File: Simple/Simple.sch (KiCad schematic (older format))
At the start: 33 parts, among them J1 IR1, J10 Conn_01x02_Female, J11 Motor1, J12 Motor2, J13 Conn_01x03_Male, J14 Conn_01x04_Male, J2 IR2, J3 IR3, J4 IR4, J5 Conn_01x03_Male, J6 Conn_01x02_Female, J7 Ultra1, J8 Ultra2, J9 Conn_01x03_Male, Q1 BSS138, Q2 BSS138, SW1 SW_Push, U1 AP7366, U2 SP485CN-L_TR, U3 ATtiny816-SS

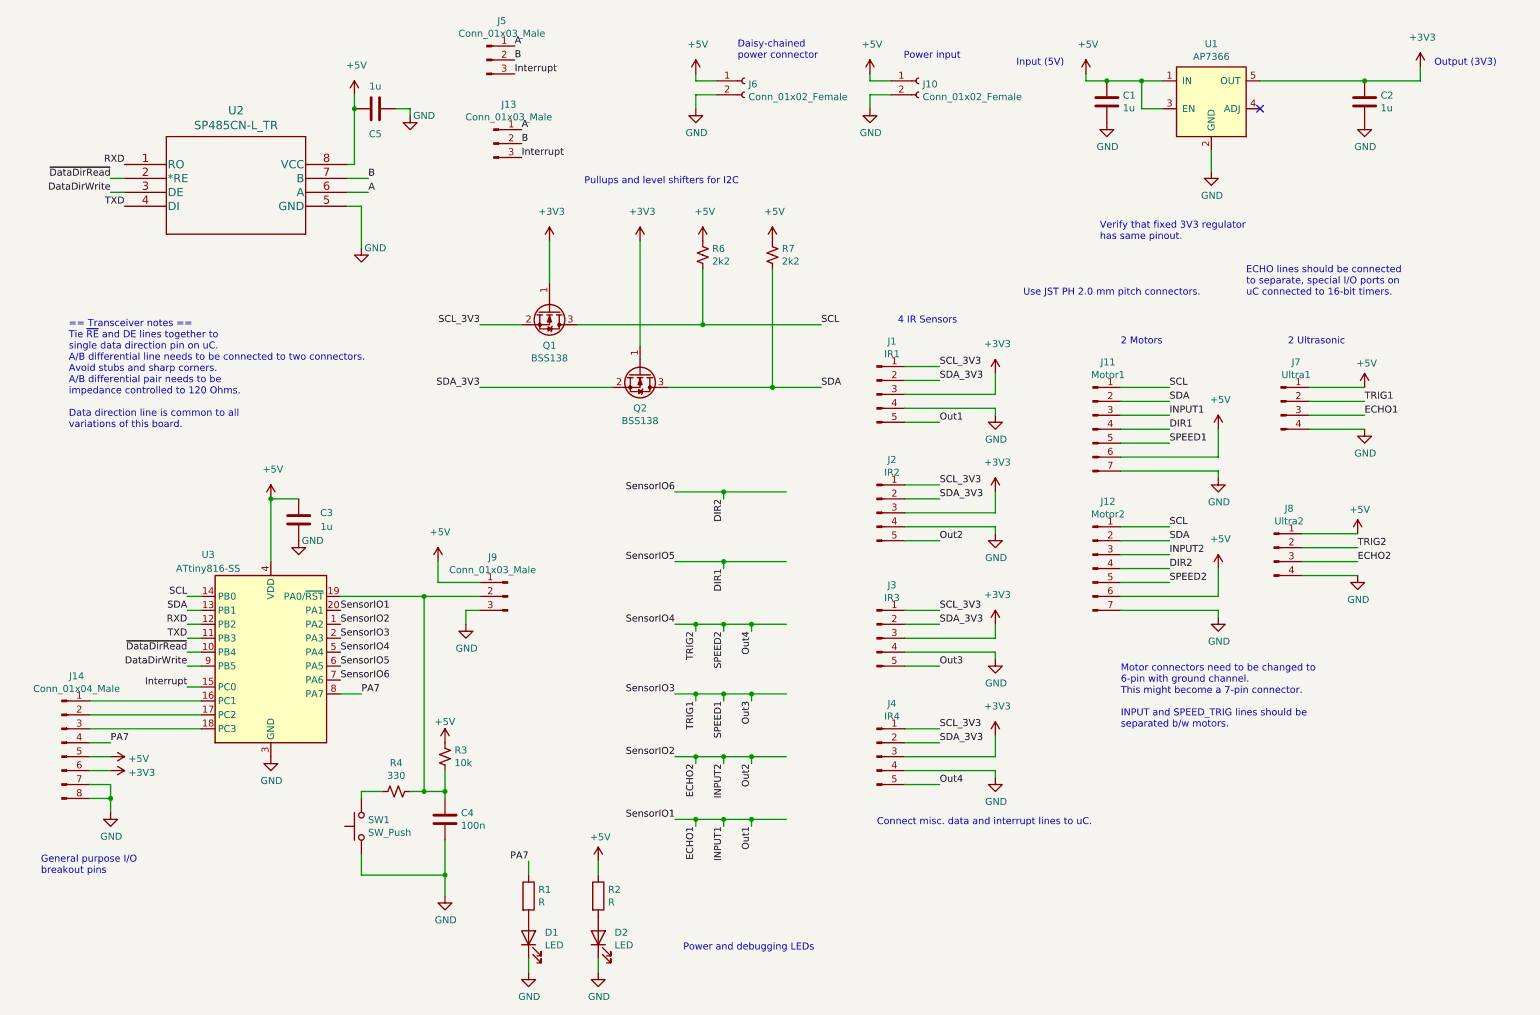
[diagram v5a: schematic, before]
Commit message: Layout started and sensor connectors are connected to eachother but not microcontroller
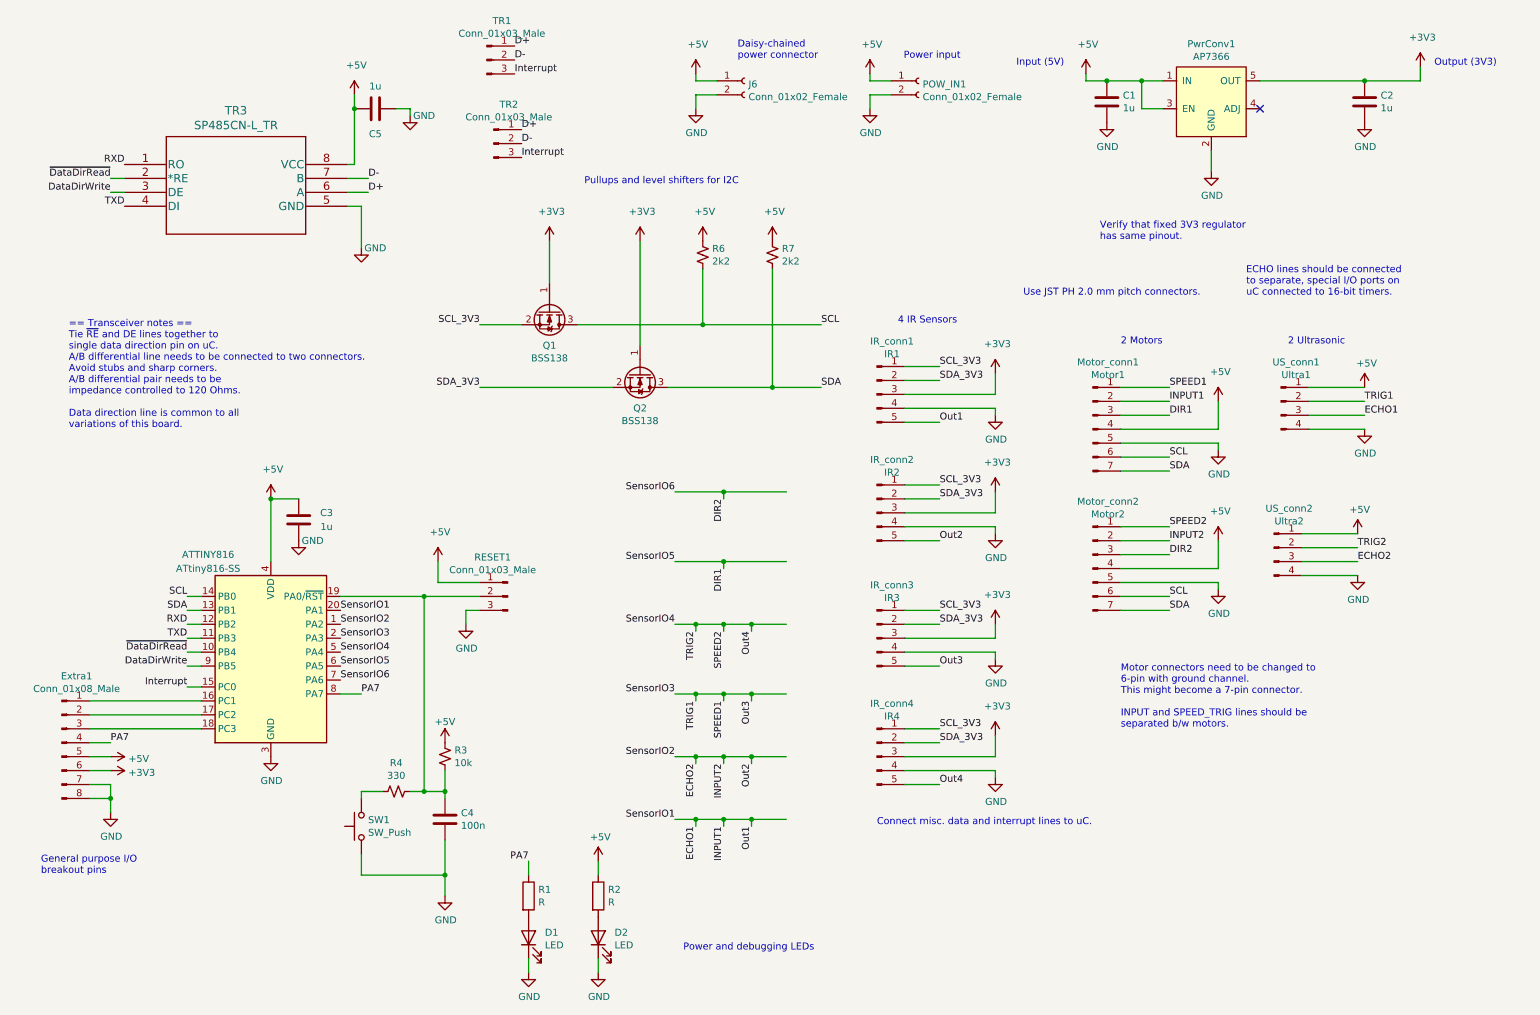
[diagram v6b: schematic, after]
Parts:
- ATTINY816: renamed from U3; footprint Package_SO:SOIC-14_3.9x8.7mm_P1.27mm -> Package_SO:SOIC-20W_7.5x12.8mm_P1.27mm
- Extra1: renamed from J14; value Conn_01x04_Male -> Conn_01x08_Male; footprint Connector_JST:JST_PH_B4B-PH-K_1x04_P2.00mm_Vertical -> Connector_JST:JST_PH_B8B-PH-K_1x08_P2.00mm_Vertical
- SW1: footprint (none) -> SimpleUCLib:SW_SPST_PTS815
- renumbered J1 to IR_conn1, J2 to IR_conn2, J3 to IR_conn3, J4 to IR_conn4, J11 to Motor_conn1, J12 to Motor_conn2, J10 to POW_IN1, U1 to PwrConv1, J9 to RESET1, J5 to TR1, J13 to TR2, U2 to TR3, J7 to US_conn1, J8 to US_conn2
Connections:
- net labels added: D+, D-
- net labels removed: A, B

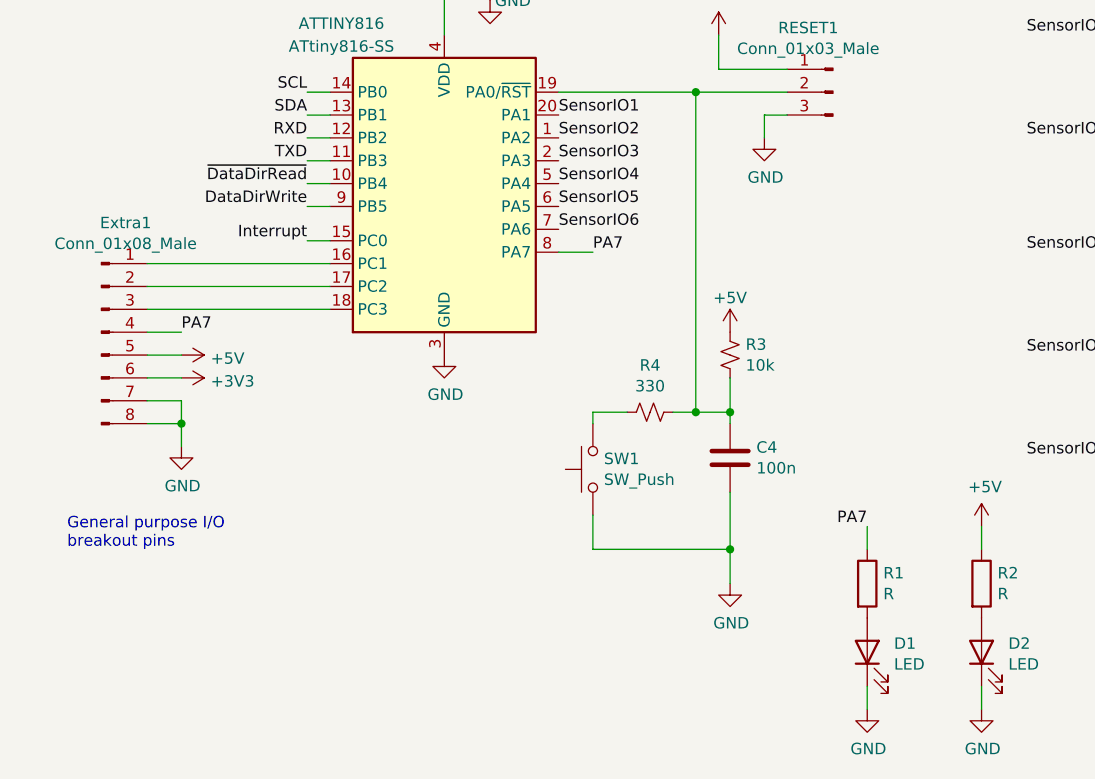
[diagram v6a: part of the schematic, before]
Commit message: rotated motor/ultrasonic connectors and added traces for all but pwr, gnd, d+/-
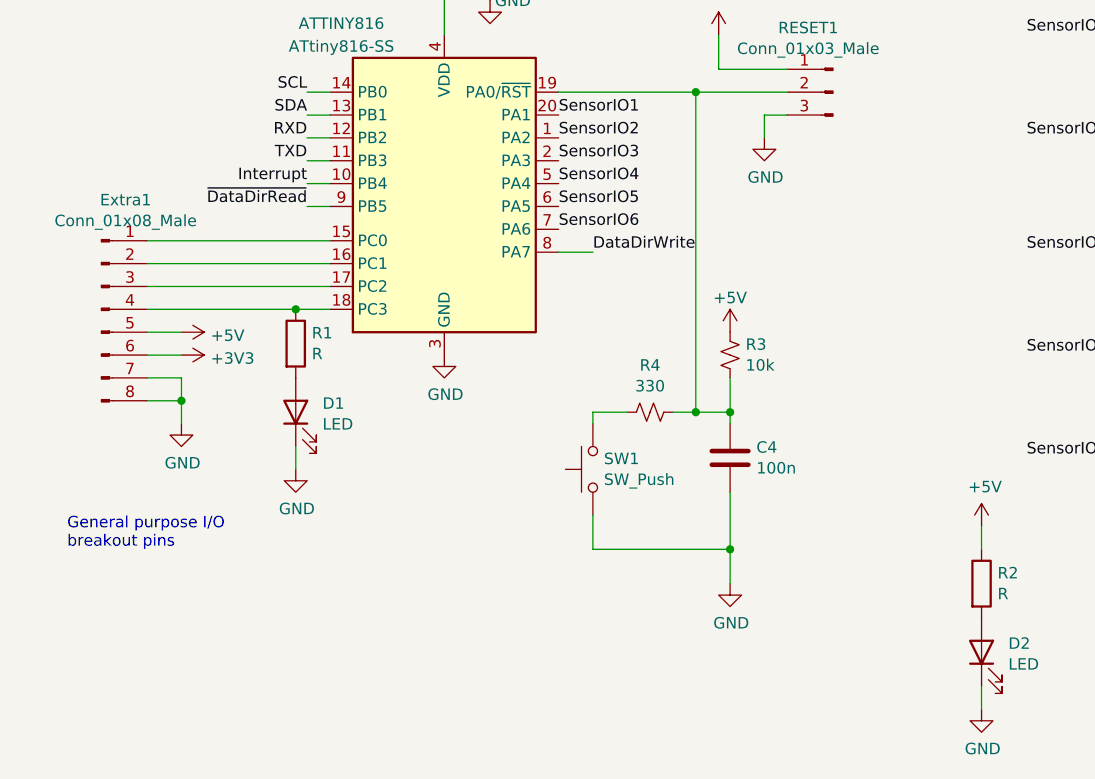
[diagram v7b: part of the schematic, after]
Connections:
- net labels removed: PA7
- wire segments 168 -> 167
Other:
- moved on the sheet: D1, Extra1, R1
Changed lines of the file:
@@
 Text Label 5200 4500 2    50   ~ 0
 SensorIO5
-Text Label 1700 5150 2    50   ~ 0
+Text Label 1700 5250 2    50   ~ 0
 ~DataDirRead
 Text Label 5200 4950 2    50   ~ 0
@@
 Text Label 4100 1600 0    50   ~ 0
 Interrupt
-Text Label 1700 5400 2    50   ~ 0
-Interrupt
 Text Label 1150 1850 2    50   ~ 0
 DataDirWrite
@@
 	1    0    0    -1
 $EndComp
-Text Label 1700 5250 2    50   ~ 0
+Text Label 2950 5450 0    50   ~ 0
 DataDirWrite
 Wire Wire Line
@@
 Wire Wire Line
 	1800 5150 1700 5150
-Wire Wire Line
-	1700 5400 1800 5400
 $Comp
 L Connector:Conn_01x08_Male Extra1
 U 1 1 6057FB03
-P 800 5800
-F 0 "Extra1" H 906 6278 50  0000 C CNN
-F 1 "Conn_01x08_Male" H 906 6187 50  0000 C CNN
-F 2 "Connector_JST:JST_PH_B8B-PH-K_1x08_P2.00mm_Vertical" H 800 5800 50  0001 C CNN
-F 3 "~" H 800 5800 50  0001 C CNN
-	1    800  5800
+P 800 5700
+F 0 "Extra1" H 906 6178 50  0000 C CNN
+F 1 "Conn_01x08_Male" H 906 6087 50  0000 C CNN
+F 2 "Connector_JST:JST_PH_B8B-PH-K_1x08_P2.00mm_Vertical" H 800 5700 50  0001 C CNN
+F 3 "~" H 800 5700 50  0001 C CNN
+	1    800  5700
 	1    0    0    -1
 $EndComp
@@
 	1800 5600 1000 5600
 Wire Wire Line
-	1000 5700 1800 5700
-Wire Wire Line
-	1000 5800 1150 5800
-Text Label 1150 5800 0    50   ~ 0
-PA7
+	1000 5700 1650 5700
 Wire Wire Line
 	2800 5450 2950 5450
-Text Label 2950 5450 0    50   ~ 0
-PA7
+Text Label 1700 5150 2    50   ~ 0
+Interrupt
 Text Notes 650  6750 0    50   ~ 0
 General purpose I/O \nbreakout pins
@@
 Daisy-chained \npower connector
 Wire Wire Line
-	1000 5900 1150 5900
-Wire Wire Line
-	1150 6000 1000 6000
-Wire Wire Line
-	1000 6100 1150 6100
+	1000 5800 1150 5800
+Wire Wire Line
+	1150 5900 1000 5900
+Wire Wire Line
+	1000 6000 1150 6000
+Wire Wire Line
+	1150 6000 1150 6100
+Wire Wire Line
+	1150 6100 1000 6100
+Connection ~ 1150 6100
 Wire Wire Line
 	1150 6100 1150 6200
-Wire Wire Line
-	1150 6200 1000 6200
-Connection ~ 1150 6200
-Wire Wire Line
-	1150 6200 1150 6300
 $Comp
 L power:GND #PWR05
 U 1 1 605D578E
-P 1150 6300
-F 0 "#PWR05" H 1150 6050 50  0001 C CNN
-F 1 "GND" H 1155 6127 50  0000 C CNN
-F 2 "" H 1150 6300 50  0001 C CNN
-F 3 "" H 1150 6300 50  0001 C CNN
-	1    1150 6300
+P 1150 6200
+F 0 "#PWR05" H 1150 5950 50  0001 C CNN
+F 1 "GND" H 1155 6027 50  0000 C CNN
+F 2 "" H 1150 6200 50  0001 C CNN
+F 3 "" H 1150 6200 50  0001 C CNN
+	1    1150 6200
 	1    0    0    -1
 $EndComp
@@
 L power:+5V #PWR03
 U 1 1 605D5831
+P 1150 5800
+F 0 "#PWR03" H 1150 5650 50  0001 C CNN
+F 1 "+5V" V 1165 5928 50  0000 L CNN
+F 2 "" H 1150 5800 50  0001 C CNN
+F 3 "" H 1150 5800 50  0001 C CNN
+	1    1150 5800
+	0    1    1    0
+$EndComp
+$Comp
+L power:+3V3 #PWR04
+U 1 1 605D5906
 P 1150 5900
-F 0 "#PWR03" H 1150 5750 50  0001 C CNN
-F 1 "+5V" V 1165 6028 50  0000 L CNN
+F 0 "#PWR04" H 1150 5750 50  0001 C CNN
+F 1 "+3V3" V 1165 6028 50  0000 L CNN
 F 2 "" H 1150 5900 50  0001 C CNN
 F 3 "" H 1150 5900 50  0001 C CNN
@@
 $EndComp
 $Comp
-L power:+3V3 #PWR04
-U 1 1 605D5906
-P 1150 6000
-F 0 "#PWR04" H 1150 5850 50  0001 C CNN
-F 1 "+3V3" V 1165 6128 50  0000 L CNN
-F 2 "" H 1150 6000 50  0001 C CNN
-F 3 "" H 1150 6000 50  0001 C CNN
-	1    1150 6000
-	0    1    1    0
-$EndComp
-$Comp
 L Device:LED D1
 U 1 1 605DF6F7
-P 4150 7200
-F 0 "D1" V 4188 7083 50  0000 R CNN
-F 1 "LED" V 4097 7083 50  0000 R CNN
-F 2 "LED_SMD:LED_0603_1608Metric" H 4150 7200 50  0001 C CNN
-F 3 "~" H 4150 7200 50  0001 C CNN
-	1    4150 7200
+P 1650 6150
+F 0 "D1" V 1688 6033 50  0000 R CNN
+F 1 "LED" V 1597 6033 50  0000 R CNN
+F 2 "LED_SMD:LED_0603_1608Metric" H 1650 6150 50  0001 C CNN
+F 3 "~" H 1650 6150 50  0001 C CNN
+	1    1650 6150
 	0    -1   -1   0
 $EndComp
@@
 L power:GND #PWR07
 U 1 1 605DF89B
-P 4150 7450
-F 0 "#PWR07" H 4150 7200 50  0001 C CNN
-F 1 "GND" H 4155 7277 50  0000 C CNN
-F 2 "" H 4150 7450 50  0001 C CNN
-F 3 "" H 4150 7450 50  0001 C CNN
-	1    4150 7450
-	1    0    0    -1
-$EndComp
-Wire Wire Line
-	4150 7450 4150 7350
+P 1650 6400
+F 0 "#PWR07" H 1650 6150 50  0001 C CNN
+F 1 "GND" H 1655 6227 50  0000 C CNN
+F 2 "" H 1650 6400 50  0001 C CNN
+F 3 "" H 1650 6400 50  0001 C CNN
+	1    1650 6400
+	1    0    0    -1
+$EndComp
+Wire Wire Line
+	1650 6400 1650 6300
 $Comp
 L Device:R R1
 U 1 1 606058D7
-P 4150 6900
-F 0 "R1" H 4220 6946 50  0000 L CNN
-F 1 "R" H 4220 6855 50  0000 L CNN
-F 2 "Resistor_SMD:R_0603_1608Metric" V 4080 6900 50  0001 C CNN
-F 3 "~" H 4150 6900 50  0001 C CNN
-	1    4150 6900
+P 1650 5850
+F 0 "R1" H 1720 5896 50  0000 L CNN
+F 1 "R" H 1720 5805 50  0000 L CNN
+F 2 "Resistor_SMD:R_0603_1608Metric" V 1580 5850 50  0001 C CNN
+F 3 "~" H 1650 5850 50  0001 C CNN
+	1    1650 5850
 	1    0    0    -1
 $EndComp
@@
 $EndComp
 Wire Wire Line
-	4150 6750 4150 6650
-Wire Wire Line
 	4650 6650 4650 6750
 $Comp
@@
 	1    0    0    -1
 $EndComp
-Text Label 4150 6650 2    50   ~ 0
-PA7
 Text Notes 6200 7300 2    50   ~ 0
 Power and debugging LEDs
@@
 	1    0    0    -1
 $EndComp
+Wire Wire Line
+	1800 5400 1000 5400
+Connection ~ 1650 5700
+Wire Wire Line
+	1650 5700 1800 5700
 $EndSCHEMATC

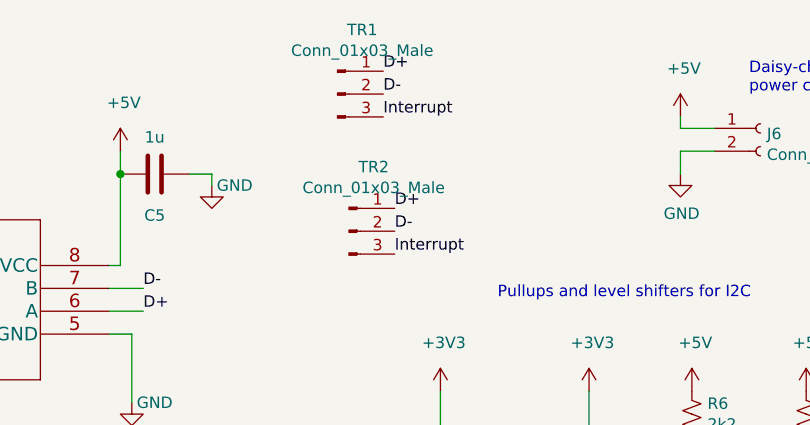
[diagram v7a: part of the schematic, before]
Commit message: minor routing changes and added pwr and gnd planes
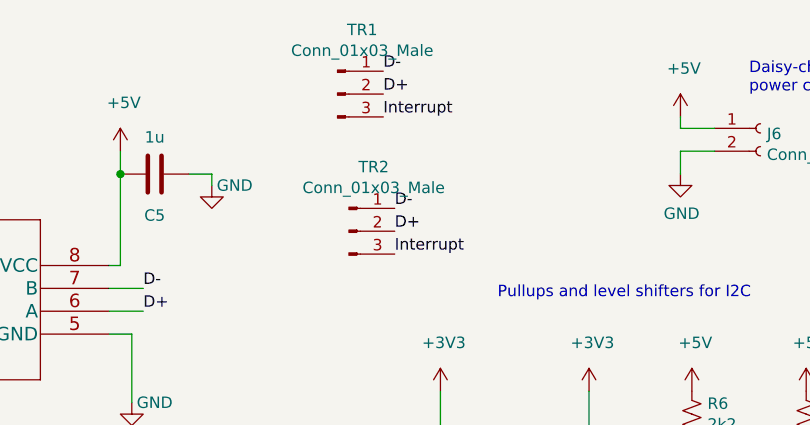
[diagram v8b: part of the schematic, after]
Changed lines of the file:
@@
 D+
 Text Label 4050 800  0    50   ~ 0
-D+
+D-
 Text Label 1250 1950 2    50   ~ 0
 TXD
@@
 $EndComp
 Text Label 4050 900  0    50   ~ 0
-D-
+D+
 Wire Wire Line
 	2300 4050 2300 4500
@@
 	1700 5050 1800 5050
 Text Label 4100 1400 0    50   ~ 0
+D-
+Text Label 4100 1500 0    50   ~ 0
 D+
-Text Label 4100 1500 0    50   ~ 0
-D-
 $Comp
 L Connector:Conn_01x03_Male TR2
